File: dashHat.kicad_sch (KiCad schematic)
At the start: 18 parts, among them J1 Input, J2 LCD, J3 GPIO, J4 LEDs, Q1 BSS138, Q2 BSS138, U1 CAT24C256

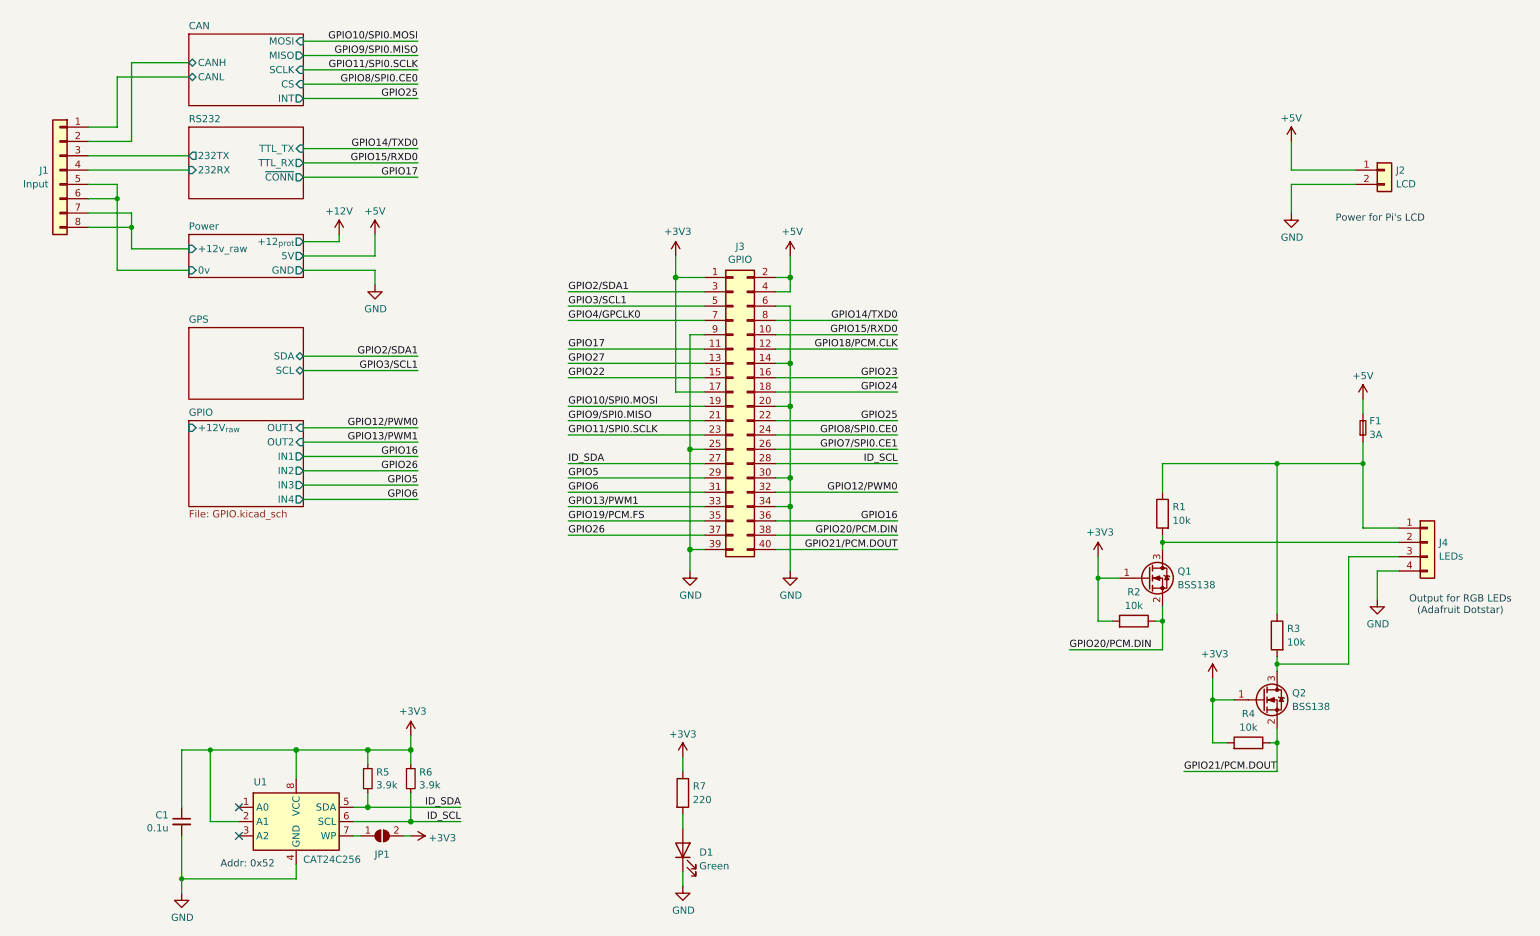
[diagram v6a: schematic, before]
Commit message: fixes from testing, updated for pi5
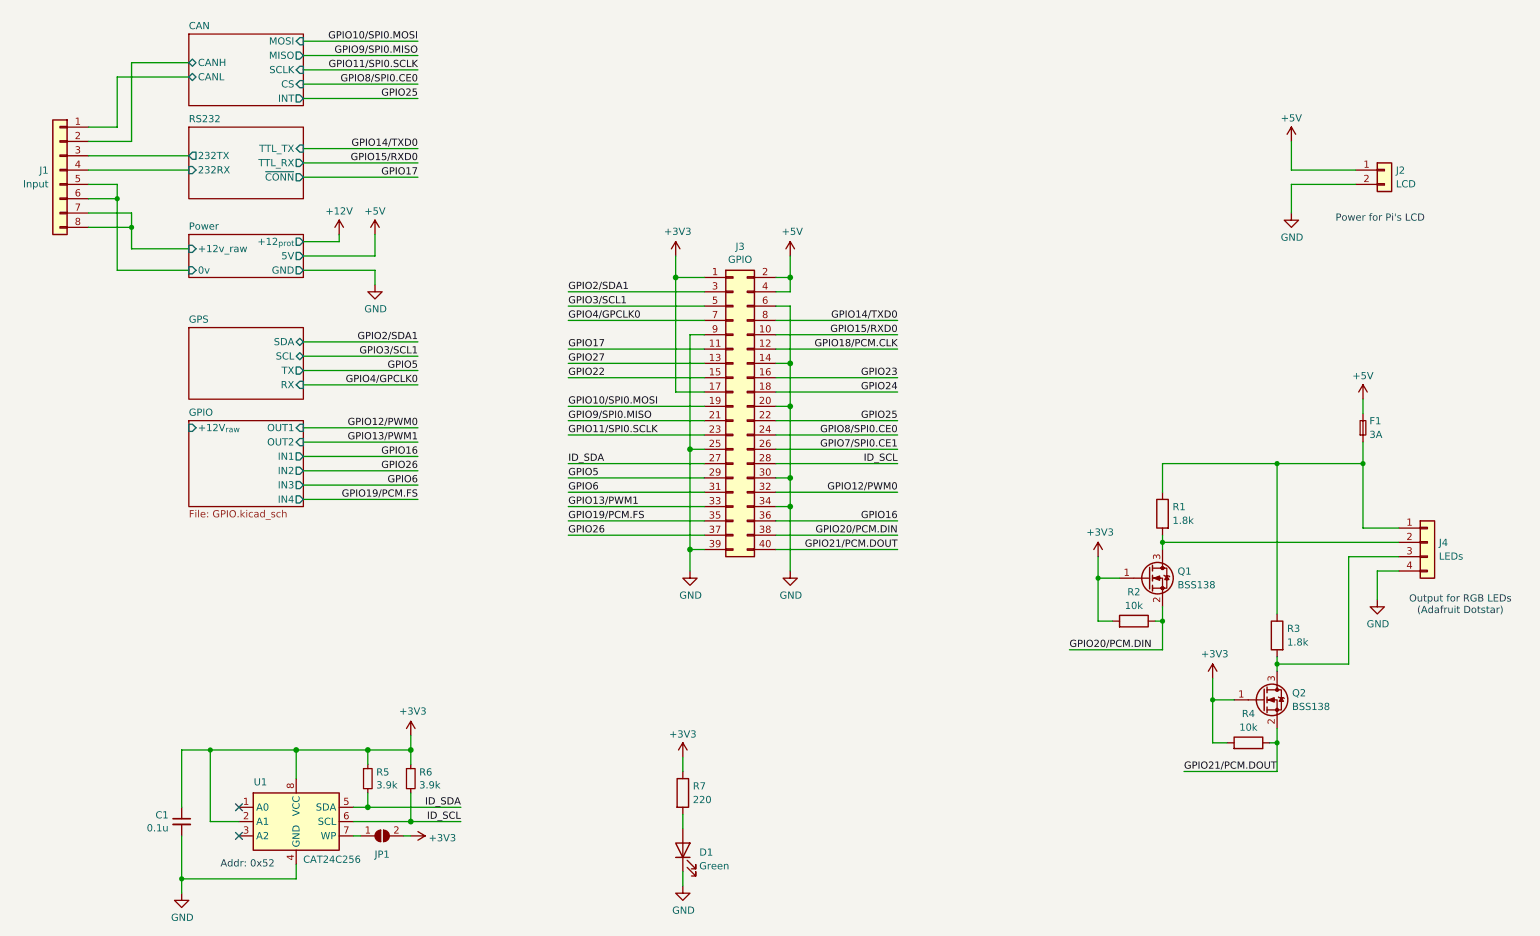
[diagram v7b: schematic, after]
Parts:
- R1, R3: value 10k -> 1.8k
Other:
- sheet GPS ports: added RX, TX; removed none
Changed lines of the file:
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@@
 	(wire
 		(pts
-			(xy 68.58 82.55) (xy 88.9 82.55)
+			(xy 68.58 80.01) (xy 88.9 80.01)
 		)
 		(stroke
@@
 	(wire
 		(pts
+			(xy 68.58 87.63) (xy 88.9 87.63)
+		)
+		(stroke
+			(width 0)
+			(type default)
+		)
+	)
+	(wire
+		(pts
 			(xy 139.7 71.12) (xy 115.57 71.12)
 		)
@@
 	(wire
 		(pts
+			(xy 68.58 85.09) (xy 88.9 85.09)
+		)
+		(stroke
+			(width 0)
+			(type default)
+		)
+	)
+	(wire
+		(pts
 			(xy 68.58 64.77) (xy 81.28 64.77)
 		)
@@
 	(wire
 		(pts
-			(xy 68.58 85.09) (xy 88.9 85.09)
+			(xy 68.58 82.55) (xy 88.9 82.55)
 		)
 		(stroke
@@
 		)
 	)
+	(label "GPIO5"
+		(at 88.9 85.09 180)
+		(fields_autoplaced yes)
+		(effects
+			(font
+				(size 1.27 1.27)
+			)
+			(justify right bottom)
+		)
+	)
 	(label "ID_SDA"
 		(at 115.57 101.6 0)
@@
 	)
 	(label "GPIO3{slash}SCL1"
-		(at 88.9 85.09 180)
+		(at 88.9 82.55 180)
 		(fields_autoplaced yes)
 		(effects
@@
 	)
 	(label "GPIO2{slash}SDA1"
-		(at 88.9 82.55 180)
+		(at 88.9 80.01 180)
 		(fields_autoplaced yes)
 		(effects
@@
 	)
 	(label "GPIO6"
-		(at 88.9 107.95 180)
+		(at 88.9 105.41 180)
 		(fields_autoplaced yes)
 		(effects
@@
 		)
 	)
-	(label "GPIO5"
-		(at 88.9 105.41 180)
+	(label "GPIO4{slash}GPCLK0"
+		(at 88.9 87.63 180)
 		(fields_autoplaced yes)
 		(effects
@@
 		)
 	)
+	(label "GPIO19{slash}PCM.FS"
+		(at 88.9 107.95 180)
+		(fields_autoplaced yes)
+		(effects
+			(font
+				(size 1.27 1.27)
+			)
+			(justify right bottom)
+		)
+	)
 	(label "GPIO25"
 		(at 88.9 36.83 180)
@@
 			)
 		)
-		(property "Value" "10k"
+		(property "Value" "1.8k"
 			(at 222.758 111.7021 0)
 			(effects
@@
 			)
 		)
-		(property "Value" "10k"
+		(property "Value" "1.8k"
 			(at 243.078 133.2921 0)
 			(effects
@@
 		)
 		(pin "SDA" bidirectional
-			(at 68.58 82.55 0)
+			(at 68.58 80.01 0)
 			(effects
 				(font
@@
 		)
 		(pin "SCL" bidirectional
+			(at 68.58 82.55 0)
+			(effects
+				(font
+					(size 1.27 1.27)
+				)
+				(justify right)
+			)
+		)
+		(pin "TX" output
 			(at 68.58 85.09 0)
 			(effects
 				(font
+					(size 1.27 1.27)
+				)
+				(justify right)
+			)
+		)
+		(pin "RX" input
+			(at 68.58 87.63 0)
+			(effects
+				(font

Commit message: added a switch to the lcd, and feedback from the 12v input to the pi
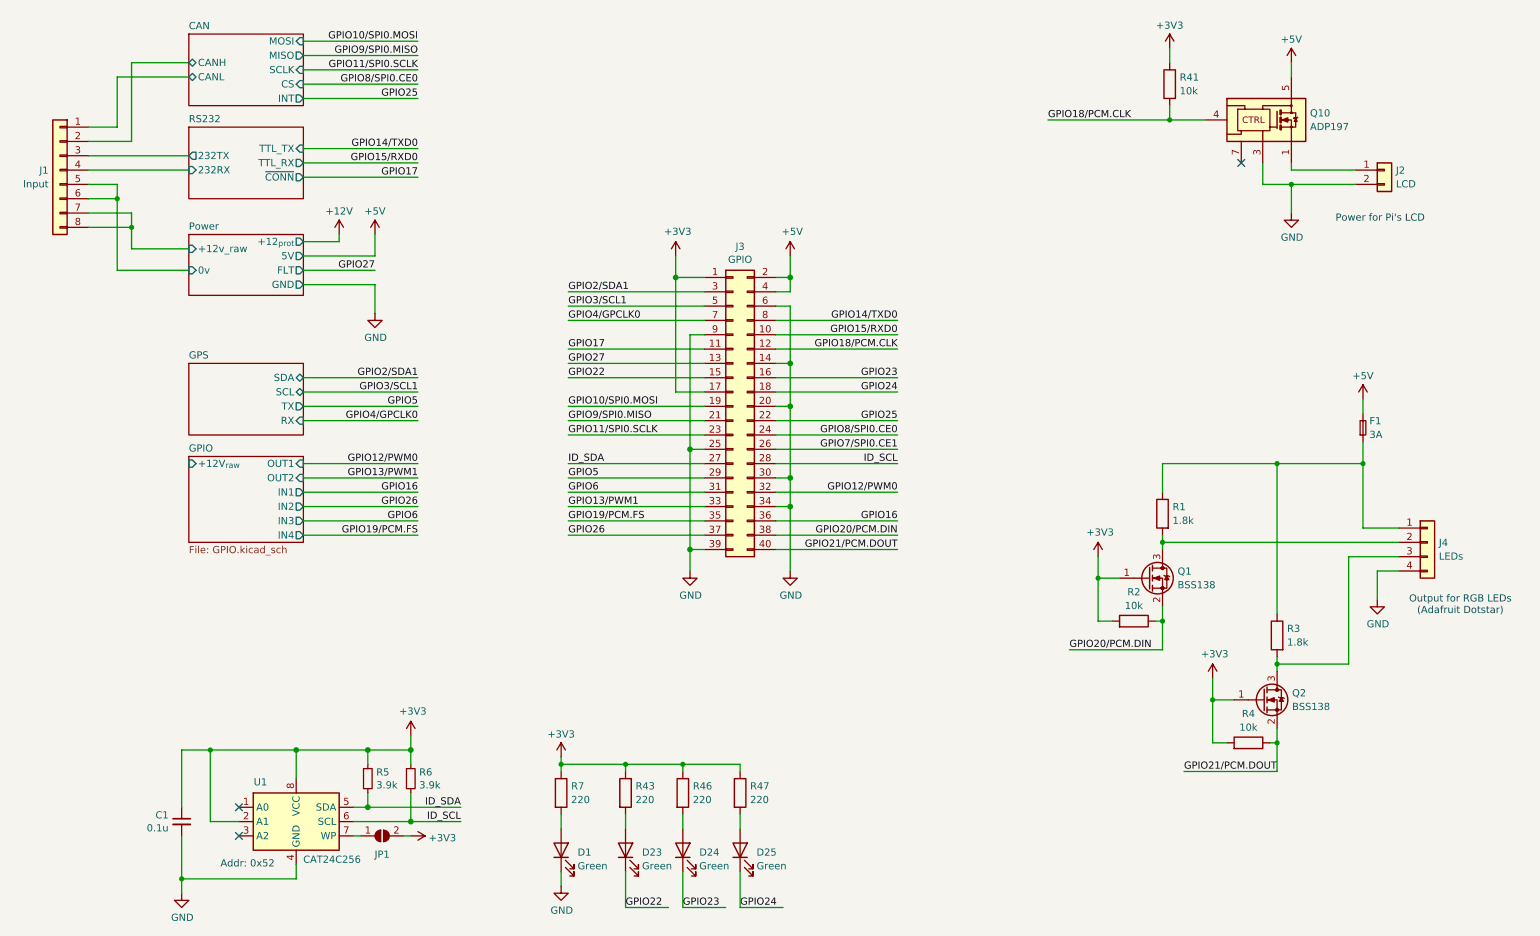
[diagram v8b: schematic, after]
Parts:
- added D23, D24, D25: Green, LED_SMD:LED_0603_1608Metric, symbol Device:LED
- added Q10: ADP197, Package_DFN_QFN:DFN-6-1EP_2x2mm_P0.65mm_EP1x1.6mm, symbol Custom:ADP197
- added R41: 10k, Resistor_SMD:R_0603_1608Metric, symbol Device:R
- added R43, R46, R47: 220, Resistor_SMD:R_0603_1608Metric, symbol Device:R
- J2: footprint Connector_JST:JST_PH_B2B-PH-K_1x02_P2.00mm_Vertical -> Connector_JST:JST_XH_B2B-XH-A_1x02_P2.50mm_Vertical
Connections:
- net +3V3: now also R41.1, R43.1, R46.1, R47.1
- net +5V: now also Q10.5 (VCC), Q10.6 (VCC); no longer J2.1 (Pin_1)
- net GND: now also Q10.3 (GND)
- net GPIO18/PCM.CLK: now also Q10.4 (EN), R41.2
- net GPIO22: now also D23.1 (K)
- net GPIO23: now also D24.1 (K)
- net GPIO24: now also D25.1 (K)
- new net: D24.2 (A), R46.2
- new net: D23.2 (A), R43.2
- new net: D25.2 (A), R47.2
- new net: J2.1 (Pin_1), Q10.1 (OUT), Q10.2 (OUT)
- no-connect marks 2 -> 3
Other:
- sheet Power ports: added FLT; removed none
- moved on the sheet: D1, R7
